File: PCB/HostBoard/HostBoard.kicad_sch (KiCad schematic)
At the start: 21 parts, among them J1 Conn_01x06, J10 Conn_01x05, J11 Screw_Terminal_01x02, J12 Conn_02x07_Odd_Even, J2 Conn_01x03, J3 Conn_01x06, J4 Conn_01x03, J5 Conn_01x06, J6 Conn_01x04, J7 Conn_01x04, J8 Conn_01x03, U1 MCP23017_SS, U2 TB6612FNG, U3 TB6612FNG

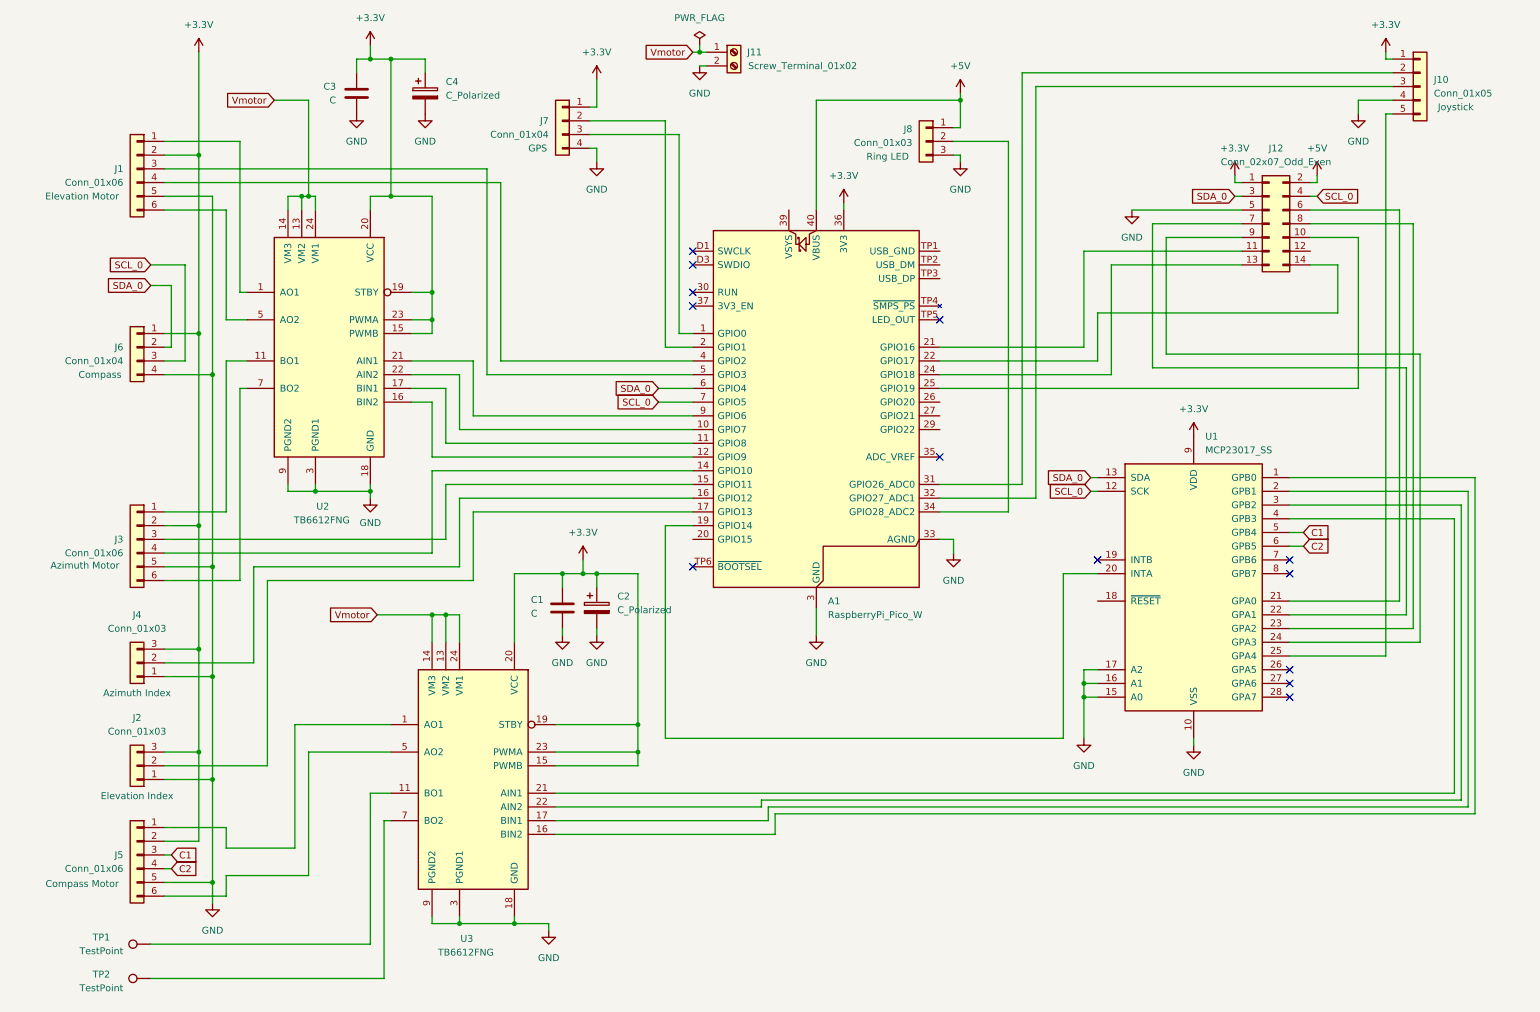
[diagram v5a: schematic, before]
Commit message: Completed PCB for existing schematic, need to re-assign LCD and check schematic
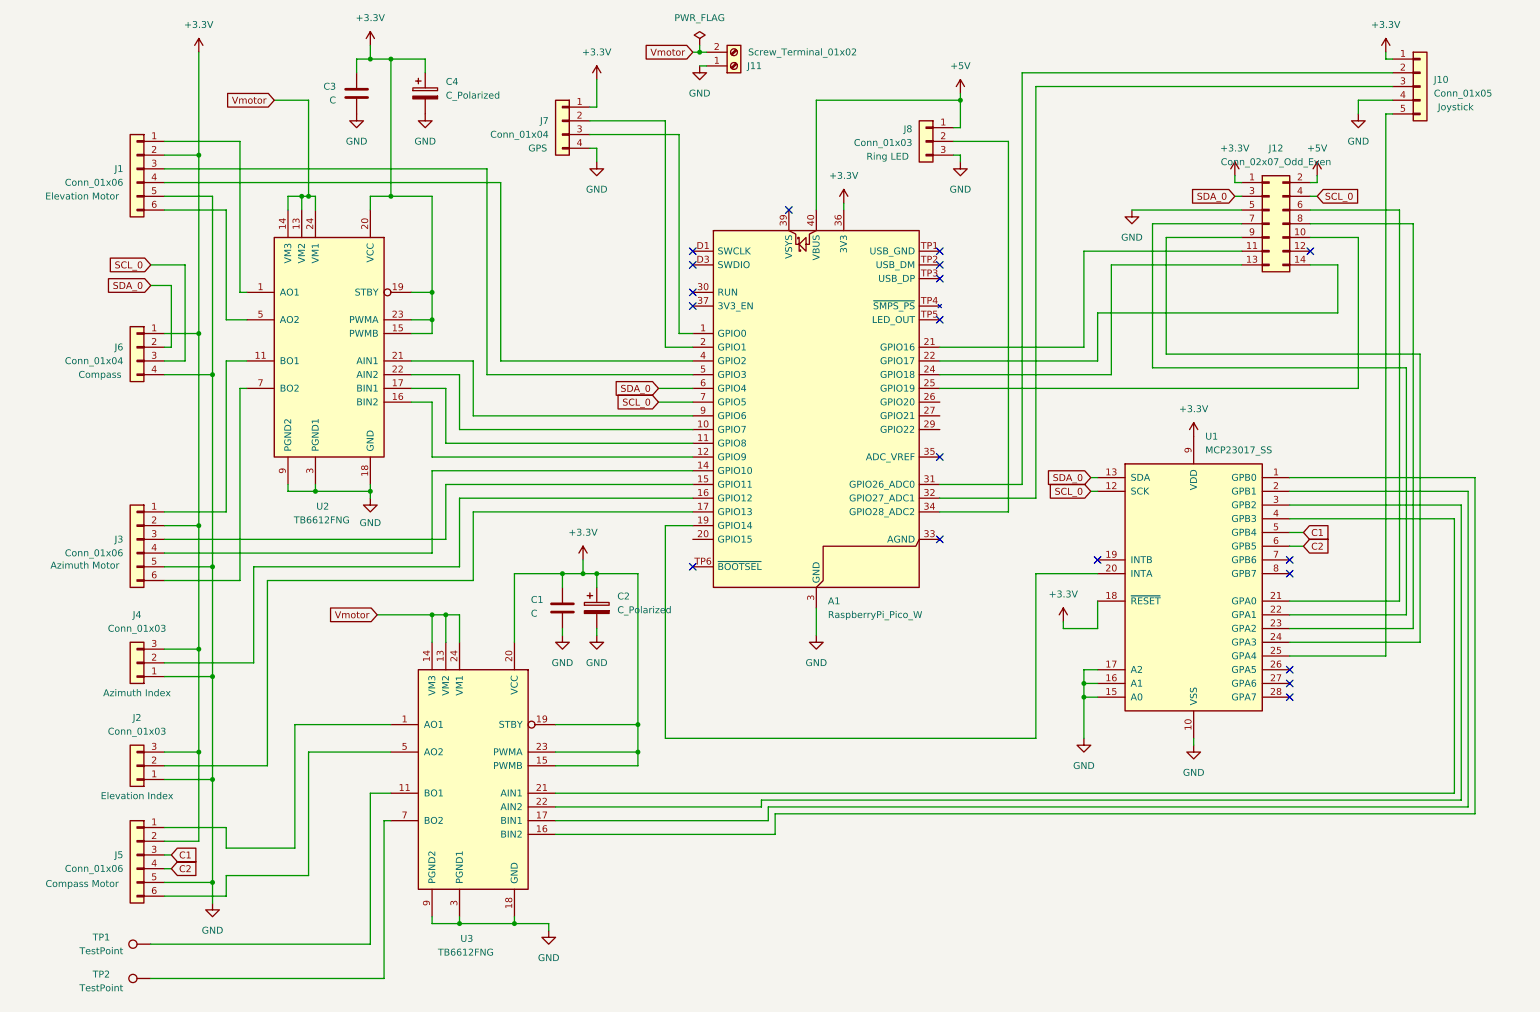
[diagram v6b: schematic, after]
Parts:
- A1: footprint Module:RaspberryPi_Pico_Common_Unspecified -> Module:RaspberryPi_Pico_Common_THT
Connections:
- net +3.3V: now also U1.18 (~{RESET})
- net GND: now also J11.1 (Pin_1); no longer A1.33 (AGND), J11.2 (Pin_2)
- net Vmotor: now also J11.2 (Pin_2); no longer J11.1 (Pin_1)
- no-connect marks 13 -> 19
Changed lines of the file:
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@@
 	)
 	(junction
+		(at 135.89 21.59)
+		(diameter 0)
+		(color 0 0 0 0)
+	)
+	(junction
 		(at 124.46 151.13)
 		(diameter 0)
@@
 	)
 	(junction
-		(at 135.89 21.59)
-		(diameter 0)
-		(color 0 0 0 0)
-	)
-	(junction
 		(at 43.18 73.66)
 		(diameter 0)
@@
 	)
 	(no_connect
+		(at 180.34 111.76)
+	)
+	(no_connect
+		(at 180.34 63.5)
+	)
+	(no_connect
 		(at 134.62 68.58)
 	)
 	(no_connect
+		(at 180.34 60.96)
+	)
+	(no_connect
+		(at 248.92 58.42)
+	)
+	(no_connect
 		(at 180.34 71.12)
 	)
@@
 	)
 	(no_connect
+		(at 152.4 50.8)
+	)
+	(no_connect
 		(at 245.11 118.11)
 	)
@@
 		(at 245.11 135.89)
 	)
+	(no_connect
+		(at 180.34 58.42)
+	)
 	(wire
 		(pts
@@
 	(wire
 		(pts
-			(xy 203.2 118.11) (xy 203.2 148.59)
+			(xy 198.12 118.11) (xy 198.12 148.59)
 		)
 		(stroke
@@
 	(wire
 		(pts
-			(xy 135.89 21.59) (xy 137.16 21.59)
-		)
-		(stroke
-			(width 0)
-			(type default)
-		)
-	)
-	(wire
-		(pts
 			(xy 86.36 99.06) (xy 86.36 114.3)
 		)
@@
 	(wire
 		(pts
-			(xy 182.88 114.3) (xy 182.88 111.76)
-		)
-		(stroke
-			(width 0)
-			(type default)
-		)
-	)
-	(wire
-		(pts
 			(xy 207.01 135.89) (xy 207.01 138.43)
 		)
@@
 	(wire
 		(pts
+			(xy 135.89 21.59) (xy 137.16 21.59)
+		)
+		(stroke
+			(width 0)
+			(type default)
+		)
+	)
+	(wire
+		(pts
 			(xy 134.62 78.74) (xy 99.06 78.74)
 		)
@@
 	(wire
 		(pts
+			(xy 203.2 128.27) (xy 203.2 127)
+		)
+		(stroke
+			(width 0)
+			(type default)
+		)
+	)
+	(wire
+		(pts
 			(xy 101.6 118.11) (xy 101.6 130.81)
 		)
@@
 	(wire
 		(pts
+			(xy 135.89 24.13) (xy 137.16 24.13)
+		)
+		(stroke
+			(width 0)
+			(type default)
+		)
+	)
+	(wire
+		(pts
 			(xy 86.36 130.81) (xy 86.36 125.73)
 		)
@@
 	(wire
 		(pts
-			(xy 264.16 25.4) (xy 195.58 25.4)
+			(xy 209.55 128.27) (xy 203.2 128.27)
 		)
 		(stroke
@@
 	(wire
 		(pts
-			(xy 88.9 93.98) (xy 88.9 83.82)
+			(xy 264.16 25.4) (xy 195.58 25.4)
 		)
 		(stroke
@@
 	(wire
 		(pts
-			(xy 135.89 24.13) (xy 137.16 24.13)
+			(xy 88.9 93.98) (xy 88.9 83.82)
 		)
 		(stroke
@@
 	(wire
 		(pts
-			(xy 129.54 148.59) (xy 203.2 148.59)
+			(xy 129.54 148.59) (xy 198.12 148.59)
 		)
 		(stroke
@@
 	(wire
 		(pts
-			(xy 203.2 118.11) (xy 209.55 118.11)
+			(xy 198.12 118.11) (xy 209.55 118.11)
 		)
 		(stroke
@@
 	(wire
 		(pts
-			(xy 40.64 60.96) (xy 34.29 60.96)
+			(xy 209.55 123.19) (xy 209.55 128.27)
 		)
 		(stroke
@@
 	(wire
 		(pts
-			(xy 45.72 175.26) (xy 45.72 179.07)
+			(xy 40.64 60.96) (xy 34.29 60.96)
 		)
 		(stroke
@@
 	(wire
 		(pts
-			(xy 91.44 104.14) (xy 91.44 116.84)
+			(xy 45.72 175.26) (xy 45.72 179.07)
 		)
 		(stroke
@@
 	(wire
 		(pts
-			(xy 182.88 111.76) (xy 180.34 111.76)
+			(xy 91.44 104.14) (xy 91.44 116.84)
 		)
 		(stroke
@@
 			)
 		)
-		(property "Footprint" "Module:RaspberryPi_Pico_Common_Unspecified"
+		(property "Footprint" "Module:RaspberryPi_Pico_Common_THT"
 			(at 157.48 135.89 0)
 			(effects
@@
 	(symbol
 		(lib_id "power:GND")
-		(at 182.88 114.3 0)
-		(unit 1)
-		(exclude_from_sim no)
-		(in_bom yes)
-		(on_board yes)
-		(dnp no)
-		(fields_autoplaced yes)
-		(property "Reference" "#PWR07"
-			(at 182.88 120.65 0)
-			(effects
-				(font
-					(size 1.27 1.27)
-				)
-				(hide yes)
-			)
-		)
-		(property "Value" "GND"
-			(at 182.88 119.38 0)
-			(effects
-				(font
-					(size 1.27 1.27)
-				)
-			)
-		)
-		(property "Footprint" ""
-			(at 182.88 114.3 0)
-			(effects
-				(font
-					(size 1.27 1.27)
-				)
-				(hide yes)
-			)
-		)
-		(property "Datasheet" ""
-			(at 182.88 114.3 0)
-			(effects
-				(font
-					(size 1.27 1.27)
-				)
-				(hide yes)
-			)
-		)
-		(property "Description" "Power symbol creates a global label with name \"GND\" , ground"
-			(at 182.88 114.3 0)
-			(effects
-				(font
-					(size 1.27 1.27)
-				)
-				(hide yes)
-			)
-		)
-		(pin "1"
-		)
-		(instances
-			(project "HostBoard"
-				(path "/08957217-e9e9-463e-9948-496b29a2ee58"
-					(reference "#PWR07")
-					(unit 1)
-				)
-			)
-		)
-	)
-	(symbol
-		(lib_id "power:GND")
 		(at 215.9 50.8 0)
 		(unit 1)
@@
 	(symbol
 		(lib_id "Connector:Screw_Terminal_01x02")
-		(at 142.24 21.59 0)
+		(at 142.24 24.13 0)
+		(mirror x)
 		(unit 1)
 		(exclude_from_sim no)
@@
 		(dnp no)
 		(property "Reference" "J11"
-			(at 146.05 21.59 0)
+			(at 146.05 24.13 0)
 			(effects
 				(font
@@
 		)
 		(property "Value" "Screw_Terminal_01x02"
-			(at 154.94 24.13 0)
+			(at 154.94 21.59 0)
 			(effects
 				(font
@@
 		)
 		(property "Footprint" "TerminalBlock:TerminalBlock_Xinya_XY308-2.54-2P_1x02_P2.54mm_Horizontal"
-			(at 142.24 21.59 0)
+			(at 142.24 24.13 0)
 			(effects
 				(font
@@
 		)
 		(property "Datasheet" "~"
-			(at 142.24 21.59 0)
+			(at 142.24 24.13 0)
 			(effects
 				(font
@@
 		)
 		(property "Description" "Generic screw terminal, single row, 01x02, script generated (kicad-library-utils/schlib/autogen/connector/)"
-			(at 142.24 21.59 0)
+			(at 142.24 24.13 0)
 			(effects
 				(font
@@
 					(unit 1)
 				)
+			)
+		)
+	)
+	(symbol
+		(lib_id "power:+3.3V")
+		(at 203.2 127 0)
+		(unit 1)
+		(exclude_from_sim no)
+		(in_bom yes)
+		(on_board yes)
+		(dnp no)
+		(fields_autoplaced yes)
+		(property "Reference" "#PWR015"
+			(at 203.2 130.81 0)
+			(effects
+				(font
+					(size 1.27 1.27)
+				)
+				(hide yes)
+			)
+		)
+		(property "Value" "+3.3V"
+			(at 203.2 121.92 0)
+			(effects
+				(font
+					(size 1.27 1.27)
+				)
+			)
+		)
+		(property "Footprint" ""
+			(at 203.2 127 0)
+			(effects
+				(font
+					(size 1.27 1.27)
+				)
+				(hide yes)
+			)
+		)
+		(property "Datasheet" ""
+			(at 203.2 127 0)
+			(effects
+				(font
+					(size 1.27 1.27)
+				)
+				(hide yes)
+			)
+		)
+		(property "Description" "Power symbol creates a global label with name \"+3.3V\""
+			(at 203.2 127 0)
+			(effects
+				(font
+					(size 1.27 1.27)
+				)
+				(hide yes)
+			)
+		)
+		(pin "1"
+		)
+		(instances
+			(project "HostBoard"
+				(path "/08957217-e9e9-463e-9948-496b29a2ee58"
+					(reference "#PWR015")
+					(unit 1)
+				)

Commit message: Moved TFT_DC and Expander INTA pins to match code
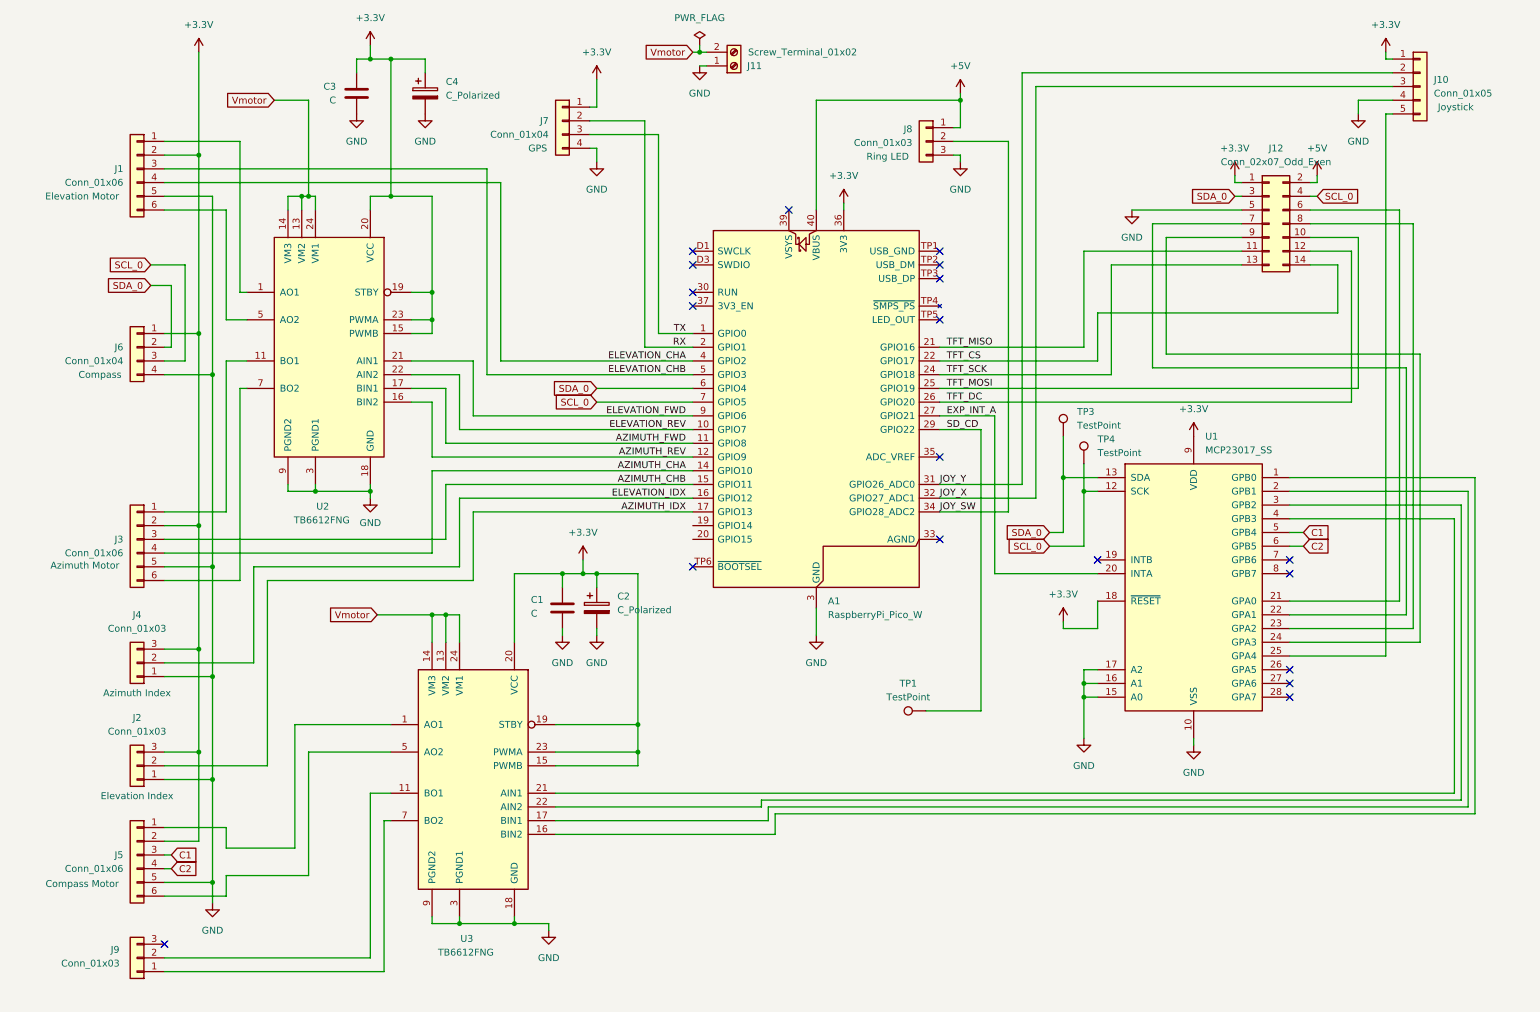
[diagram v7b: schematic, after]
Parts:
- removed TP2: TestPoint, TestPoint:TestPoint_THTPad_2.5x2.5mm_Drill1.2mm, symbol Connector:TestPoint
- added J9: Conn_01x03, Connector_PinHeader_2.54mm:PinHeader_1x03_P2.54mm_Vertical, symbol Connector_Generic:Conn_01x03
- added TP3, TP4: TestPoint, TestPoint:TestPoint_Pad_1.0x1.0mm, symbol Connector:TestPoint
- TP1: footprint TestPoint:TestPoint_THTPad_2.5x2.5mm_Drill1.2mm -> Connector_PinHeader_2.54mm:PinHeader_1x01_P2.54mm_Vertical
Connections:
- net SCL_0: now also TP4.1
- net SDA_0: now also TP3.1
- net at U3.11 (BO1), U3.12 (BO1): now also J9.2 (Pin_2); no longer TP1.1
- net at U3.7 (BO2), U3.8 (BO2): now also J9.1 (Pin_1)
- net RX: now reaches A1.2 (GPIO1), J7.2 (Pin_2)
- net TX: now reaches A1.1 (GPIO0), J7.3 (Pin_3)
- net AZIMUTH_REV: now reaches A1.12 (GPIO9), U2.16 (BIN2)
- net AZIMUTH_FWD: now reaches A1.11 (GPIO8), U2.17 (BIN1)
- net ELEVATION_FWD: now reaches A1.9 (GPIO6), U2.21 (AIN1)
- net ELEVATION_REV: now reaches A1.10 (GPIO7), U2.22 (AIN2)
- net AZIMUTH_CHB: now reaches A1.15 (GPIO11), J3.3 (Pin_3)
- net AZIMUTH_CHA: now reaches A1.14 (GPIO10), J3.4 (Pin_4)
- net ELEVATION_IDX: now reaches A1.16 (GPIO12), J4.2 (Pin_2)
- net AZIMUTH_IDX: now reaches A1.17 (GPIO13), J2.2 (Pin_2)
- net at A1.19 (GPIO14): no longer U1.20 (INTA)
- net TFT_MISO: now reaches A1.21 (GPIO16), J12.11 (Pin_11)
- net TFT_CS: now reaches A1.22 (GPIO17), J12.14 (Pin_14)
- net TFT_SCK: now reaches A1.24 (GPIO18), J12.13 (Pin_13)
- net TFT_MOSI: now reaches A1.25 (GPIO19), J12.10 (Pin_10)
- net TFT_DC: now reaches A1.26 (GPIO20)
- net TFT_DC: now also J12.12 (Pin_12)
- net EXP_INT_A: now reaches A1.27 (GPIO21)
- net EXP_INT_A: now also U1.20 (INTA)
- net SD_CD: now reaches A1.29 (GPIO22)
- net SD_CD: now also TP1.1
- net JOY_Y: now reaches A1.31 (GPIO26_ADC0), J10.2 (Pin_2)
- net JOY_X: now reaches A1.32 (GPIO27_ADC1), J10.3 (Pin_3)
- net JOY_SW: now reaches A1.34 (GPIO28_ADC2), J8.2 (Pin_2)
- net ELEVATION_CHA: now reaches A1.4 (GPIO2), J1.4 (Pin_4)
- net ELEVATION_CHB: now reaches A1.5 (GPIO3), J1.3 (Pin_3)
